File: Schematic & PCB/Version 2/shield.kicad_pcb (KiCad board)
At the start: 2 copper layers, 68.5 x 53.5 mm, 27 parts, among them J1 CONN_POWER, J2 CONN_POWER_H, P1 CONN_SENSOR_SERIAL, P2 CONN_SENSOR_SERIAL_H, P3 CONN_PROG, Q1 ZVN4206A, U1 SN74LVC245A, U2 ESP-01v090, U3 ESP-12, U4 LD1117S33CTR

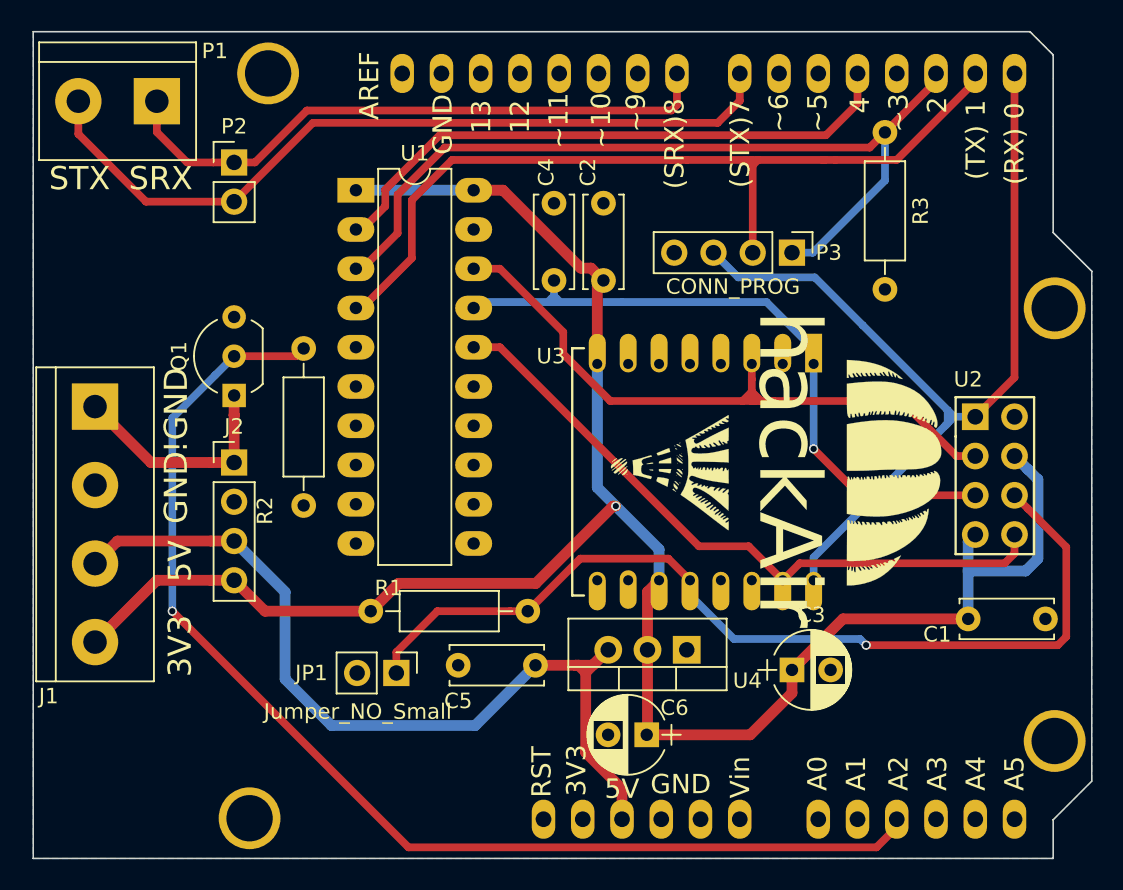
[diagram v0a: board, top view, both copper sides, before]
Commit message: Shield design revision (v2.2)
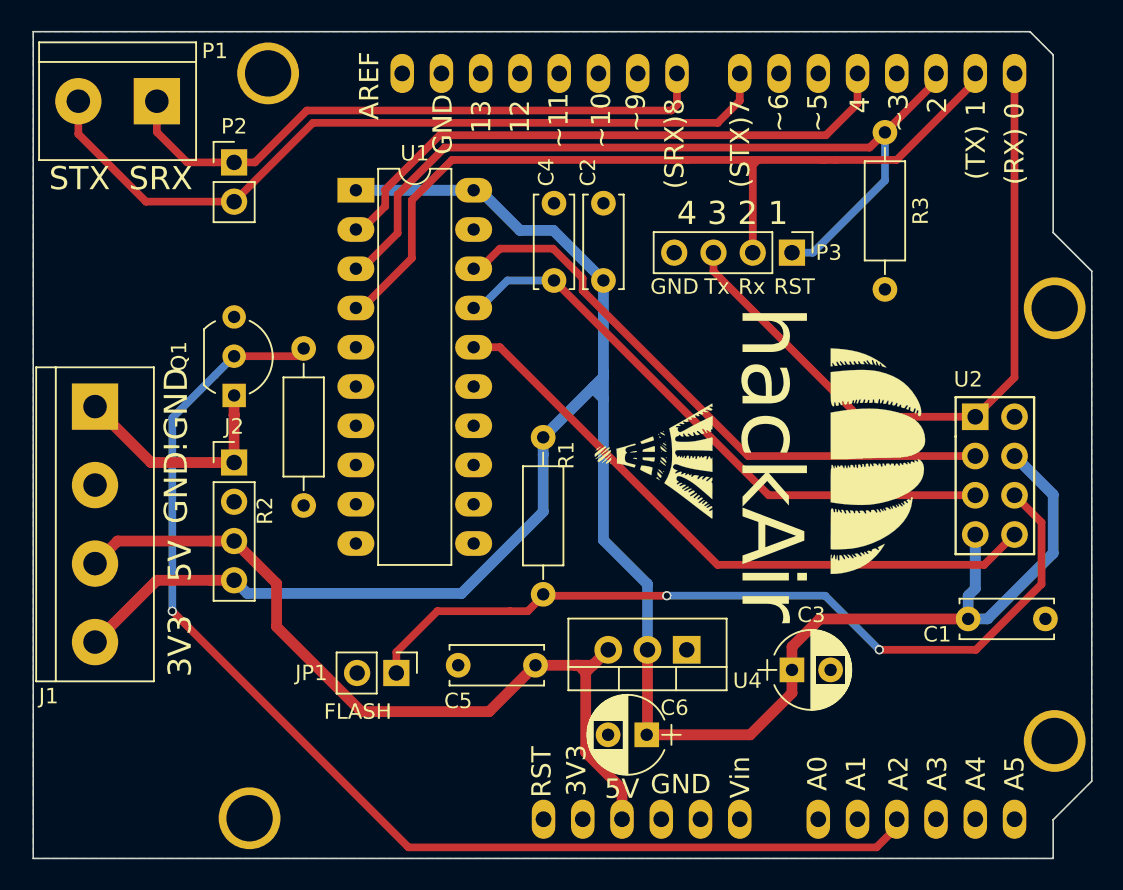
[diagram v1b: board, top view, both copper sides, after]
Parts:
- removed U3: ESP-12, ESP8266:ESP-12
- JP1: value Jumper_NO_Small -> FLASH
- Q1: footprint TO_SOT_Packages_THT:TO-92_Inline_Wide -> lib:TO-92_Inline_Wide_FlipSilk
- moved G*** 8.39 mm to (195.0, 78.8)
- moved R1 1.48 mm to (181.5, 87.9), turned to 90 degrees
- moved G*** 1.29 mm to (195.2, 79.2)
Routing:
- net /ESP_TX: track 60.0 -> 45.3 mm
- net +3V3: track 132.3 -> 139.8 mm, vias 1 -> 0
- net /ESP_IO_0: track 60.9 -> 54.3 mm, vias 1 -> 2
- net /ESP_RST: track 45.5 -> 39.5 mm, vias 1 -> 0
- net /ESP_CS: track 42.6 -> 39.0 mm
- net +5V: track 57.5 -> 55.1 mm
- net /ESP_RX: track 43.2 -> 41.6 mm
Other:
- board text added: "4 3 2 1"
- board text added: "Rx"
- board text added: "Tx"
- board text added: "hackAir WiFi Air Quality shield - Version 2.2"
- board text removed: "hackAir WiFi Air Quality shield - Version 2"
